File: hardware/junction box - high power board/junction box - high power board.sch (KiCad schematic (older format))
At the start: 19 parts, among them J1 Conn_01x04_Female, J10 Conn_01x02_Female, J2 Conn_01x04_Male, J3 Conn_01x02_Female, J4 Conn_01x02_Male, J5 Conn_01x02_Female, J6 Conn_01x02_Male, J7 Conn_01x02_Female, J8 Conn_01x02_Male, J9 Conn_01x02_Male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

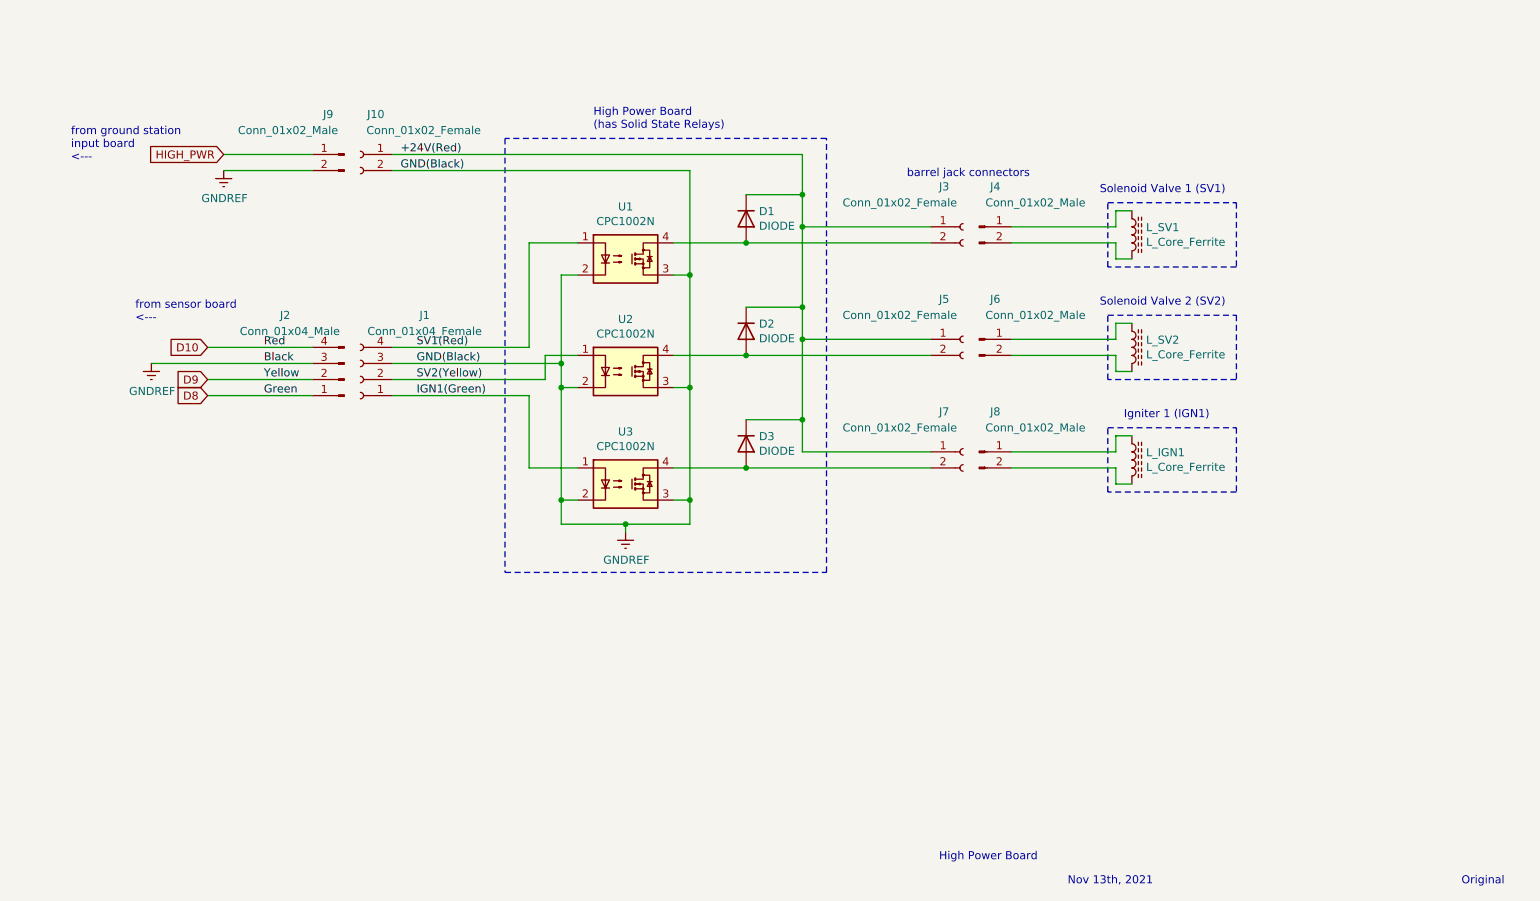
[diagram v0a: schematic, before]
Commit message: Updated Ground Station board, Junction Box sensor board, and Junction Box high power board.
Moved Ground Station pins so that abort (STOP), backup abort (BACKUP_STOP),  auto/manual launch (LAUNCH_MANL_OR_AUTO), and arming (ARM_ROCKET) signals now each go to an Arduino pin that can handle external interrupts. Shifted the rest of the pins so that the manual control pins for SV1, SV2, and IGN1 all connect to the same header on the Arduino. Added battery and outlet for extension cord to key switch circuit. Removed some male header pins because red radio XBee board must connect to them on Arduino instead. As  a consequence, the armed status buzzer/LED pins connect to male headers a level below the board using wires. XBee board also blocks nearest 5V/GND pins, so power must be obtained from the very end of the
Arduino Mega board, using external wires connected to male headers.

Added fuses to high power board. One fuse for each solid state relay, and one fuse from the main 24V high power line.

Corrected wiring for GND, D9, and D8 on sensor board's 4 pin connector (which controls the high power board). Also added a header symbol for the SDA/SCL lines, to indicate that the connections must jump a to a lower board level, down to the Arduino headers, using wires.
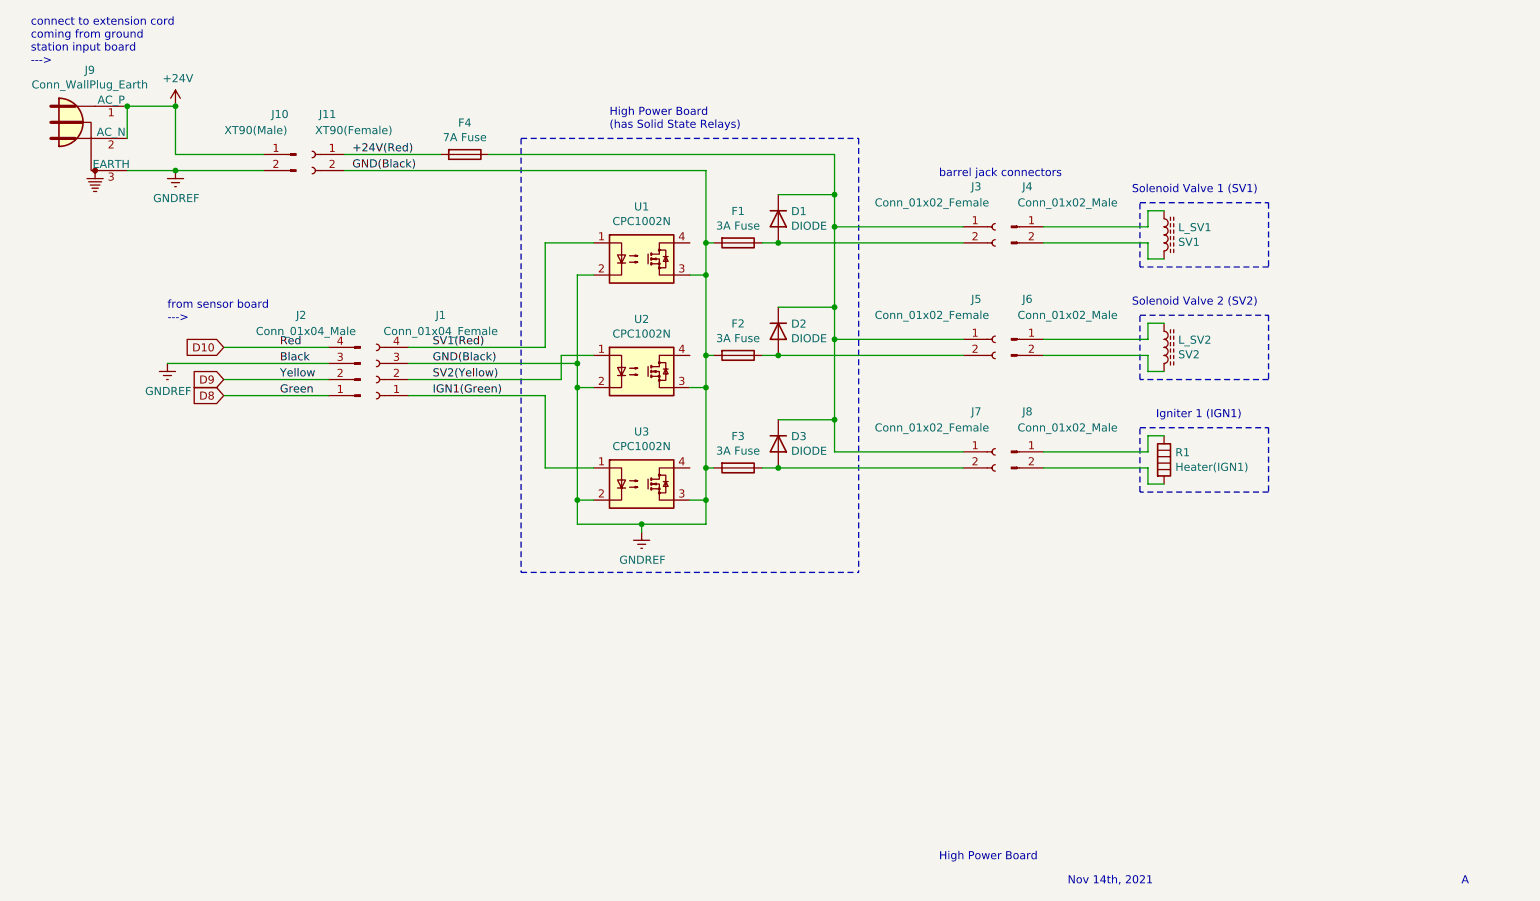
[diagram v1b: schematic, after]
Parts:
- removed L_IGN1: L_Core_Ferrite, symbol Device:L_Core_Ferrite
- added F1, F2, F3: 3A Fuse, symbol Device:Fuse
- added F4: 7A Fuse, symbol Device:Fuse
- added J9: Conn_WallPlug_Earth, symbol Connector:Conn_WallPlug_Earth
- added R1: Heater(IGN1), symbol Device:Heater
- J10: renamed from J9; value Conn_01x02_Male -> XT90(Male)
- J11: renamed from J10; value Conn_01x02_Female -> XT90(Female)
- L_SV1: value L_Core_Ferrite -> SV1
- L_SV2: value L_Core_Ferrite -> SV2
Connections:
- net +24V(Red): now also F4.2; no longer D1.2 (K), D2.2 (K), D3.2 (K), J3.1 (Pin_1), J5.1 (Pin_1), J7.1 (Pin_1)
- net GNDREF: now also F1.2, F2.2, F3.2, J9.3 (EARTH)
- net at D1.1 (A), J3.2 (Pin_2): now also F1.1; no longer U1.4
- net at D2.1 (A), J5.2 (Pin_2): now also F2.1; no longer U2.4
- net at D3.1 (A), J7.2 (Pin_2): now also F3.1; no longer U3.4
- net at J8.1 (Pin_1): now also R1.1
- net at J8.2 (Pin_2): now also R1.2
- net HIGH_PWR renamed +24V
- net +24V: now also J9.1 (AC_P), J9.2 (AC_N)
- new net: D1.2 (K), D2.2 (K), D3.2 (K), F4.1, J3.1 (Pin_1), J5.1 (Pin_1), J7.1 (Pin_1)
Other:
- note added: "A"
- note added: "Nov 14th, 2021"
- note added: "connect to extension cord \ncoming from ground \nstation input board\n--->"
- note added: "from sensor board\n--->"
- note removed: "Nov 13th, 2021"
- note removed: "Original"
- note removed: "from ground station\ninput board\n<---"
- note removed: "from sensor board\n<---"
- moved on the sheet: D1, D2, D3, J1, J10, J11, J2, J3, J4, J5, J6, J7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
